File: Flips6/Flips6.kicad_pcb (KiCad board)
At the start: 2 copper layers, 100 x 50 mm, 25 parts, among them CN1 Conn_02x04_Odd_Even, IC1 74595, IC2 74595, IC3 74595

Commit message: Switching back to V0.9
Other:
- board text added: "SRT Flips 6 V0.9 2018-11-16 github.com/cawapy/FlipSuite"
- board text removed: "SRT Flips 6 V1.0 2018-11-16 github.com/cawapy/FlipSuite"
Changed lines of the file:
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@@
     (title "Flips 6")
     (date 2018-11-16)
-    (rev V1.0)
+    (rev V0.9)
     (company SRT)
     (comment 1 "Serial 2+6 FP2800A Port Controller")
@@
   (gr_line (start 230.505 78.105) (end 239.395 78.105) (layer F.SilkS) (width 0.1))
   (gr_line (start 240.665 78.105) (end 249.555 78.105) (layer F.SilkS) (width 0.1))
-  (gr_text "SRT Flips 6 V1.0 2018-11-16\ngithub.com/cawapy/FlipSuite" (at 190.5 104.775) (layer F.SilkS)
+  (gr_text "SRT Flips 6 V0.9 2018-11-16\ngithub.com/cawapy/FlipSuite" (at 190.5 104.775) (layer F.SilkS)
     (effects (font (size 1.5 1.5) (thickness 0.3)) (justify left))
   )

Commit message: adding shift register pin mapping
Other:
- board text added: "(Shift) Register Pin Mapping:"
- board text added: "0 1 2"
- board text added: "0 YA.0 XA.0 X3EN"
- board text added: "1 YA.1 XA.1 X4EN"
- board text added: "2 YA.2 XA.2 X5EN"
- board text added: "3 YB.0 XB.0 X6EN"
- board text added: "4 YB.1 XB.1"
- board text added: "5 YDAT XDAT"
- board text added: "6 Y1EN X1EN"
- board text added: "7 Y2EN X2EN"
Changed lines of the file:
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@@
-(kicad_pcb (version 20171130) (host pcbnew "(5.0.1)-3")
+(kicad_pcb (version 20171130) (host pcbnew "(5.0.1)-4")
   (general
     (thickness 1.6)
-    (drawings 73)
+    (drawings 99)
     (tracks 760)
     (zones 0)
@@
   )
   (layers
-    (0 F.Cu signal hide)
+    (0 F.Cu signal)
     (31 B.Cu signal)
     (32 B.Adhes user)
@@
     )
   )
+  (gr_line (start 247.65 73.025) (end 247.65 75.565) (layer B.SilkS) (width 0.1))
+  (gr_line (start 240.03 73.025) (end 240.03 75.565) (layer B.SilkS) (width 0.1))
+  (gr_line (start 201.93 67.945) (end 201.93 73.025) (layer B.SilkS) (width 0.1))
+  (gr_line (start 224.79 73.025) (end 224.79 75.565) (layer B.SilkS) (width 0.1))
+  (gr_line (start 209.55 67.945) (end 209.55 73.025) (layer B.SilkS) (width 0.1))
+  (gr_line (start 217.17 67.945) (end 217.17 73.025) (layer B.SilkS) (width 0.1))
+  (gr_line (start 232.41 67.945) (end 232.41 75.565) (layer B.SilkS) (width 0.1))
+  (gr_line (start 259.715 73.025) (end 194.31 73.025) (angle 90) (layer B.SilkS) (width 0.1))
+  (gr_line (start 259.715 70.485) (end 259.715 73.025) (angle 90) (layer B.SilkS) (width 0.1))
+  (gr_line (start 194.31 70.485) (end 259.715 70.485) (angle 90) (layer B.SilkS) (width 0.1))
+  (gr_line (start 259.715 67.945) (end 194.31 67.945) (angle 90) (layer B.SilkS) (width 0.2))
+  (gr_line (start 255.27 65.405) (end 255.27 75.565) (angle 90) (layer B.SilkS) (width 0.2))
+  (gr_line (start 194.31 65.405) (end 259.715 65.405) (angle 90) (layer B.SilkS) (width 0.2))
+  (gr_line (start 194.31 75.565) (end 194.31 65.405) (angle 90) (layer B.SilkS) (width 0.2))
+  (gr_line (start 259.715 75.565) (end 194.31 75.565) (angle 90) (layer B.SilkS) (width 0.2))
+  (gr_line (start 259.715 65.405) (end 259.715 75.565) (angle 90) (layer B.SilkS) (width 0.2))
+  (gr_text "(Shift) Register Pin Mapping:" (at 259.08 62.865) (layer B.SilkS)
+    (effects (font (size 1.5 1.5) (thickness 0.3)) (justify left mirror))
+  )
+  (gr_text "7\nY2EN\nX2EN\n " (at 201.295 70.485) (layer B.SilkS)
+    (effects (font (size 1.5 1.5) (thickness 0.3)) (justify left mirror))
+  )
+  (gr_text "6   \nY1EN\nX1EN\n " (at 208.915 70.485) (layer B.SilkS)
+    (effects (font (size 1.5 1.5) (thickness 0.3)) (justify left mirror))
+  )
+  (gr_text "5   \nYDAT\nXDAT\n " (at 216.535 70.485) (layer B.SilkS)
+    (effects (font (size 1.5 1.5) (thickness 0.3)) (justify left mirror))
+  )
+  (gr_text "4   \nYB.1\nXB.1\n " (at 224.155 70.485) (layer B.SilkS)
+    (effects (font (size 1.5 1.5) (thickness 0.3)) (justify left mirror))
+  )
+  (gr_text "3   \nYB.0\nXB.0\nX6EN" (at 231.775 70.485) (layer B.SilkS)
+    (effects (font (size 1.5 1.5) (thickness 0.3)) (justify left mirror))
+  )
+  (gr_text "2   \nYA.2\nXA.2\nX5EN" (at 239.395 70.485) (layer B.SilkS)
+    (effects (font (size 1.5 1.5) (thickness 0.3)) (justify left mirror))
+  )
+  (gr_text "1   \nYA.1\nXA.1\nX4EN" (at 247.015 70.485) (layer B.SilkS)
+    (effects (font (size 1.5 1.5) (thickness 0.3)) (justify left mirror))
+  )
+  (gr_text "0   \nYA.0\nXA.0\nX3EN" (at 254.635 70.485) (layer B.SilkS)
+    (effects (font (size 1.5 1.5) (thickness 0.3)) (justify left mirror))
+  )
+  (gr_text "\n0\n1\n2" (at 259.08 70.485) (layer B.SilkS)
+    (effects (font (size 1.5 1.5) (thickness 0.3)) (justify left mirror))
+  )
   (gr_line (start 260.985 78.105) (end 269.875 78.105) (layer F.SilkS) (width 0.1))

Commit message: Changing pin names in mapping table on back side silk screen
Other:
- board text added: "(Shift) Register Pin Mapping"
- board text added: "0 Y.A0 X.A0 X3.EN"
- board text added: "1 Y.A1 X.A1 X4.EN"
- board text added: "2 Y.A2 X.A2 X5.EN"
- board text added: "3 Y.B0 X.B0 X6.EN"
- board text added: "4 Y.B1 X.B1"
- board text added: "5 Y.DAT X.DAT"
- board text added: "6 Y1.EN X1.EN"
- board text added: "7 Y2.EN X2.EN"
- board text removed: "(Shift) Register Pin Mapping:"
- board text removed: "0 YA.0 XA.0 X3EN"
- board text removed: "1 YA.1 XA.1 X4EN"
- board text removed: "2 YA.2 XA.2 X5EN"
- board text removed: "3 YB.0 XB.0 X6EN"
- board text removed: "4 YB.1 XB.1"
- board text removed: "5 YDAT XDAT"
- board text removed: "6 Y1EN X1EN"
- board text removed: "7 Y2EN X2EN"
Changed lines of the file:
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@@
   (gr_line (start 259.715 75.565) (end 194.31 75.565) (angle 90) (layer B.SilkS) (width 0.2))
   (gr_line (start 259.715 65.405) (end 259.715 75.565) (angle 90) (layer B.SilkS) (width 0.2))
-  (gr_text "(Shift) Register Pin Mapping:" (at 259.08 62.865) (layer B.SilkS)
+  (gr_text "(Shift) Register Pin Mapping" (at 259.08 62.865) (layer B.SilkS)
     (effects (font (size 1.5 1.5) (thickness 0.3)) (justify left mirror))
   )
-  (gr_text "7\nY2EN\nX2EN\n " (at 201.295 70.485) (layer B.SilkS)
+  (gr_text "7\nY2.EN\nX2.EN\n " (at 201.295 70.485) (layer B.SilkS)
     (effects (font (size 1.5 1.5) (thickness 0.3)) (justify left mirror))
   )
-  (gr_text "6   \nY1EN\nX1EN\n " (at 208.915 70.485) (layer B.SilkS)
+  (gr_text "6   \nY1.EN\nX1.EN\n " (at 208.915 70.485) (layer B.SilkS)
     (effects (font (size 1.5 1.5) (thickness 0.3)) (justify left mirror))
   )
-  (gr_text "5   \nYDAT\nXDAT\n " (at 216.535 70.485) (layer B.SilkS)
+  (gr_text "5   \nY.DAT\nX.DAT\n " (at 216.535 70.485) (layer B.SilkS)
     (effects (font (size 1.5 1.5) (thickness 0.3)) (justify left mirror))
   )
-  (gr_text "4   \nYB.1\nXB.1\n " (at 224.155 70.485) (layer B.SilkS)
+  (gr_text "4   \nY.B1\nX.B1\n " (at 224.155 70.485) (layer B.SilkS)
     (effects (font (size 1.5 1.5) (thickness 0.3)) (justify left mirror))
   )
-  (gr_text "3   \nYB.0\nXB.0\nX6EN" (at 231.775 70.485) (layer B.SilkS)
+  (gr_text "3   \nY.B0\nX.B0\nX6.EN" (at 231.775 70.485) (layer B.SilkS)
     (effects (font (size 1.5 1.5) (thickness 0.3)) (justify left mirror))
   )
-  (gr_text "2   \nYA.2\nXA.2\nX5EN" (at 239.395 70.485) (layer B.SilkS)
+  (gr_text "2   \nY.A2\nX.A2\nX5.EN" (at 239.395 70.485) (layer B.SilkS)
     (effects (font (size 1.5 1.5) (thickness 0.3)) (justify left mirror))
   )
-  (gr_text "1   \nYA.1\nXA.1\nX4EN" (at 247.015 70.485) (layer B.SilkS)
+  (gr_text "1   \nY.A1\nX.A1\nX4.EN" (at 247.015 70.485) (layer B.SilkS)
     (effects (font (size 1.5 1.5) (thickness 0.3)) (justify left mirror))
   )
-  (gr_text "0   \nYA.0\nXA.0\nX3EN" (at 254.635 70.485) (layer B.SilkS)
+  (gr_text "0   \nY.A0\nX.A0\nX3.EN" (at 254.635 70.485) (layer B.SilkS)
     (effects (font (size 1.5 1.5) (thickness 0.3)) (justify left mirror))
   )

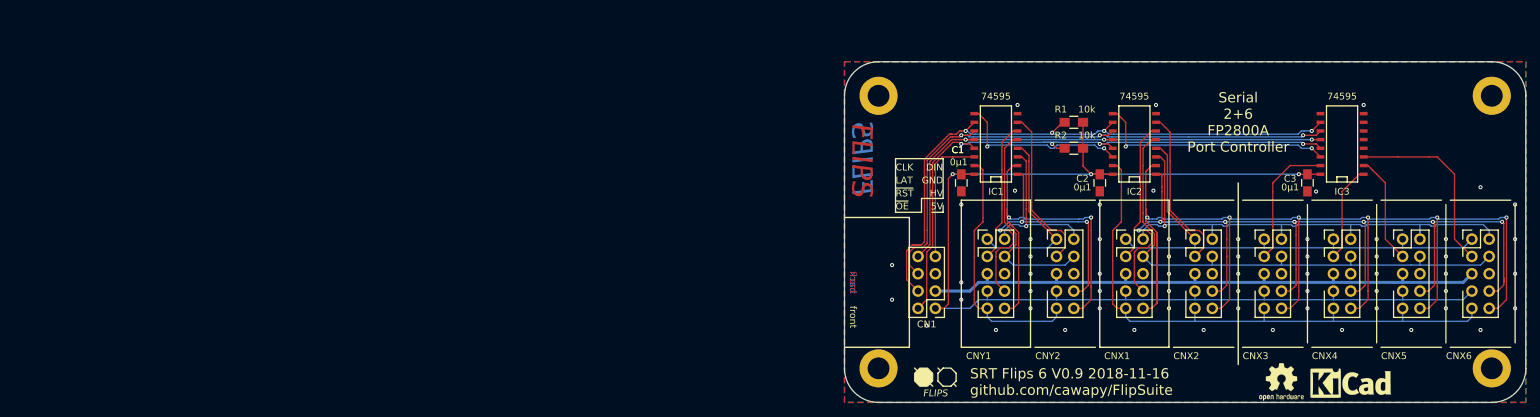
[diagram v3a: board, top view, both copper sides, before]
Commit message: move pcb to (2 in | 2 in)
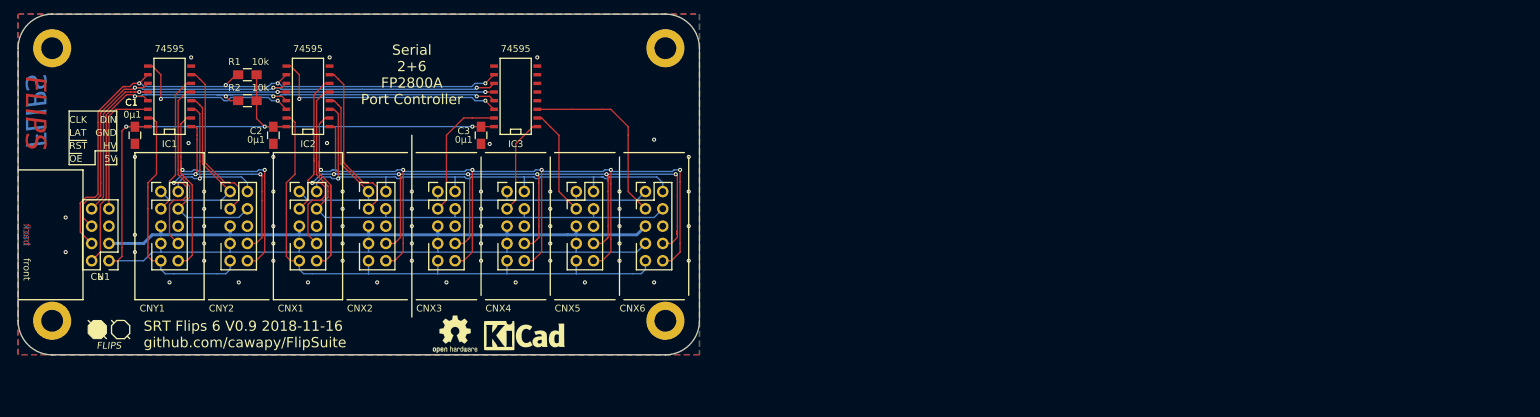
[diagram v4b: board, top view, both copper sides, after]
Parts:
- removed the REF** at (177.1, 102.8)
- removed the REF** at (267.1, 102.8)
- removed the REF** at (267.1, 62.8)
- removed the REF** at (177.1, 62.8)
- added REF**: MountingHole_3.2mm_M3_DIN965_Pad, Mounting_Holes:MountingHole_3.2mm_M3_DIN965_Pad, F.Cu at (55.8, 95.8)
- added REF**: MountingHole_3.2mm_M3_DIN965_Pad, Mounting_Holes:MountingHole_3.2mm_M3_DIN965_Pad, F.Cu at (145.8, 95.8)
- added REF**: MountingHole_3.2mm_M3_DIN965_Pad, Mounting_Holes:MountingHole_3.2mm_M3_DIN965_Pad, F.Cu at (145.8, 55.8)
- added REF**: MountingHole_3.2mm_M3_DIN965_Pad, Mounting_Holes:MountingHole_3.2mm_M3_DIN965_Pad, F.Cu at (55.8, 55.8)
- moved CNX6 121.5 mm to (142.9, 76.8)
- moved C2 121.5 mm to (88.3, 68.6)
- moved CNX1 121.5 mm to (92.1, 76.8)
- moved CNX2 121.5 mm to (102.2, 76.8)
- moved CNX3 121.5 mm to (112.4, 76.8)
- moved IC3 121.5 mm to (123.8, 62.9)
- moved R1 121.5 mm to (84.5, 59.7)
- moved R2 121.5 mm to (84.5, 63.5)
- moved C1 121.5 mm to (67.9, 68.6)
- moved C3 121.5 mm to (118.7, 68.6)
- moved CNX4 121.5 mm to (122.6, 76.8)
- moved CNX5 121.5 mm to (132.7, 76.8)
- moved CNY1 121.5 mm to (71.8, 76.8)
- moved IC1 121.5 mm to (73.0, 62.9)
- moved IC2 121.5 mm to (93.3, 62.9)
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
